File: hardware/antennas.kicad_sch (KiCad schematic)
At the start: 21 parts, among them J1001 132134

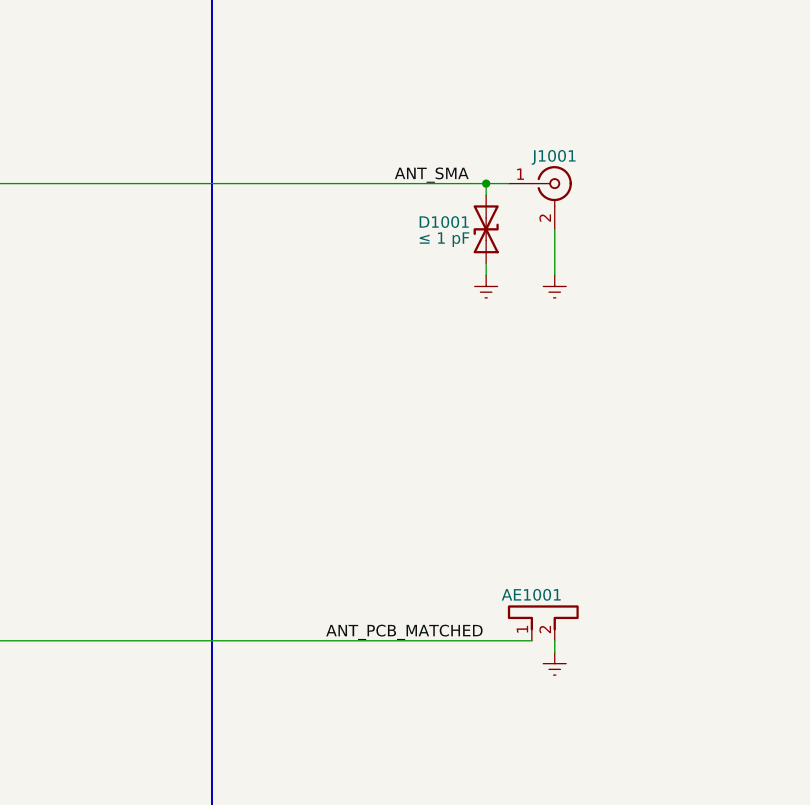
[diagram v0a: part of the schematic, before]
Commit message: HW: Update libraries, fix typos, refine schematics
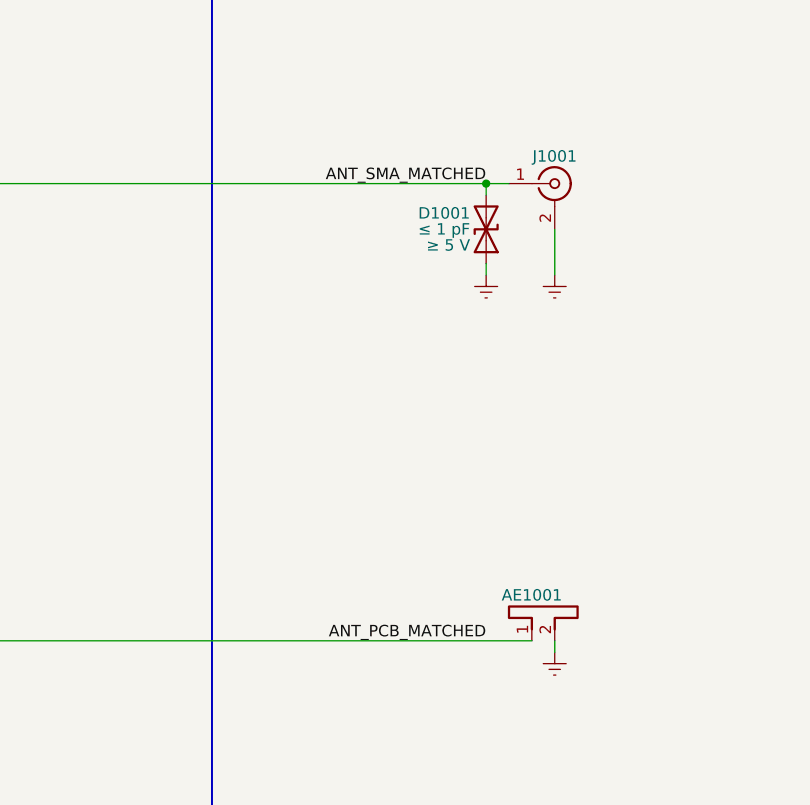
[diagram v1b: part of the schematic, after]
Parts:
- D1001: Voltage (none) -> ≥ 5 V
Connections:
- net ANT_SMA renamed ANT_SMA_MATCHED
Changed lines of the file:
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@@
 	)
 	(label "ANT_PCB_MATCHED"
-		(at 342.9 205.74 0)
+		(at 360.68 205.74 180)
 		(effects
 			(font
 				(size 1.27 1.27)
 			)
-			(justify left bottom)
+			(justify right bottom)
 		)
 	)
@@
 		)
 	)
-	(label "ANT_SMA"
-		(at 350.52 154.94 0)
+	(label "ANT_SMA_MATCHED"
+		(at 360.68 154.94 180)
 		(effects
 			(font
 				(size 1.27 1.27)
 			)
-			(justify left bottom)
+			(justify right bottom)
 		)
 	)
@@
 		(dnp no)
 		(property "Reference" "D1001"
-			(at 358.902 159.258 90)
+			(at 358.902 158.242 90)
 			(effects
 				(font
@@
 			)
 		)
-		(property "Size" ""
-			(at 358.394 162.052 90)
-			(effects
-				(font
-					(size 1.27 1.27)
-				)
-				(justify right)
-			)
-		)
-		(property "Capacitance" "≤ 1 pF"
-			(at 358.902 161.036 90)
-			(effects
-				(font
-					(size 1.27 1.27)
-				)
-				(justify right)
-			)
-		)
 		(property "Footprint review check" "+"
 			(at 360.68 160.02 90)
@@
 			)
 		)
-		(property "Power" ""
-			(at 360.68 160.02 90)
-			(effects
-				(font
-					(size 1.27 1.27)
-				)
-				(hide yes)
-			)
-		)
+		(property "Capacitance" "≤ 1 pF"
+			(at 358.902 160.02 90)
+			(effects
+				(font
+					(size 1.27 1.27)
+				)
+				(justify right)
+			)
+		)
+		(property "Voltage" "≥ 5 V"
+			(at 358.902 161.798 90)
+			(effects
+				(font
+					(size 1.27 1.27)
+				)
+				(justify right)
+			)
+		)

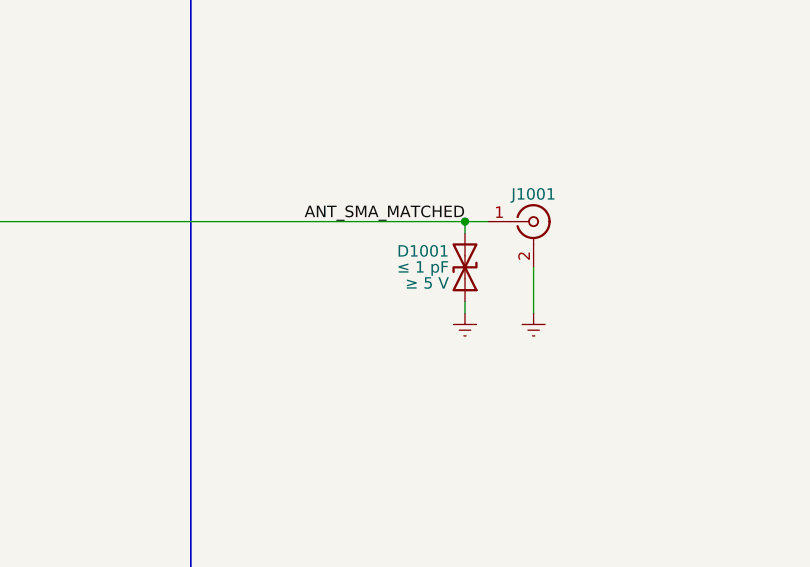
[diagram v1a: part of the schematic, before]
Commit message: HW: Update date and ANT_SMA TVS voltage rating
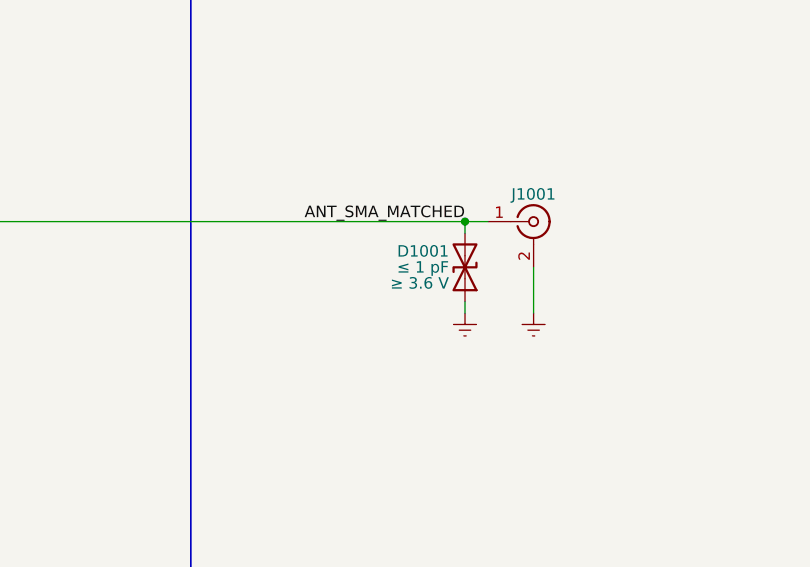
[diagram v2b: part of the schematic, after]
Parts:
- D1001: Voltage ≥ 5 V -> ≥ 3.6 V
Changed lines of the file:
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@@
 	(title_block
 		(title "Iida devkit")
-		(date "2025-05-21")
+		(date "2025-05-23")
 		(rev "v5.0.0")
 	)
@@
 			)
 		)
-		(property "Voltage" "≥ 5 V"
+		(property "Voltage" "≥ 3.6 V"
 			(at 358.902 161.798 90)
 			(effects

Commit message: HW: Refine schematics
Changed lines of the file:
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@@
 	(title_block
 		(title "Iida devkit")
-		(date "2025-05-23")
+		(date "2025-05-24")
 		(rev "v5.0.0")
 	)
@@
 	)
 	(label "ANT_SEL_PCB"
-		(at 76.2 205.74 0)
+		(at 88.9 205.74 0)
 		(effects
 			(font
@@
 	)
 	(label "ANT_SEL_SMA"
-		(at 76.2 154.94 0)
-		(effects
-			(font
+		(at 88.9 154.94 0)
+		(effects
+			(font

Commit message: HW: Fix BOM
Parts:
- C1001, C1005: DigiKey Part Number 490-11194-1-ND -> 732-13231-1-ND; MPN GJM1555C1H1R1WB01D -> 885392005006; Manufacturer Murata Electronics -> Würth Elektronik
- C1003: DigiKey Part Number 490-GJM1555C1HR33WB01DCT-ND -> 732-13226-1-ND; MPN GJM1555C1HR33WB01D -> 885392005001; Manufacturer Murata Electronics -> Würth Elektronik
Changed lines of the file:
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@@
 			)
 		)
-		(property "DigiKey Part Number" "490-11194-1-ND"
+		(property "DigiKey Part Number" "732-13231-1-ND"
 			(at 213.36 205.74 90)
 			(effects
@@
 			)
 		)
-		(property "MPN" "GJM1555C1H1R1WB01D"
+		(property "MPN" "885392005006"
 			(at 213.36 205.74 90)
 			(effects
@@
 			)
 		)
-		(property "Manufacturer" "Murata Electronics"
+		(property "Manufacturer" "Würth Elektronik"
 			(at 213.36 205.74 90)
 			(effects
@@
 			)
 		)
-		(property "DigiKey Part Number" "490-11194-1-ND"
+		(property "DigiKey Part Number" "732-13231-1-ND"
 			(at 134.62 205.74 90)
 			(effects
@@
 			)
 		)
-		(property "MPN" "GJM1555C1H1R1WB01D"
+		(property "MPN" "885392005006"
 			(at 134.62 205.74 90)
 			(effects
@@
 			)
 		)
-		(property "Manufacturer" "Murata Electronics"
+		(property "Manufacturer" "Würth Elektronik"
 			(at 134.62 205.74 90)
 			(effects
@@
 			)
 		)
-		(property "DigiKey Part Number" "490-GJM1555C1HR33WB01DCT-ND"
+		(property "DigiKey Part Number" "732-13226-1-ND"
 			(at 173.99 205.74 90)
 			(effects
@@
 			)
 		)
-		(property "MPN" "GJM1555C1HR33WB01D"
+		(property "MPN" "885392005001"
 			(at 173.99 205.74 90)
 			(effects
@@
 			)
 		)
-		(property "Manufacturer" "Murata Electronics"
+		(property "Manufacturer" "Würth Elektronik"
 			(at 173.99 205.74 90)
 			(effects

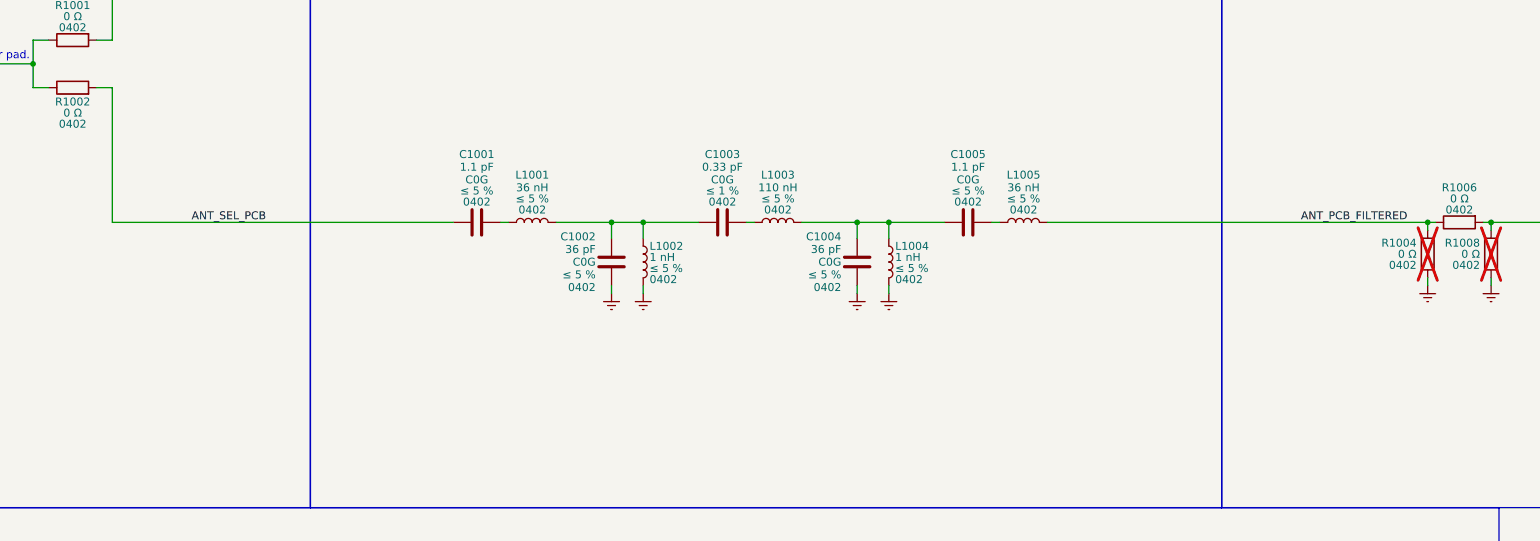
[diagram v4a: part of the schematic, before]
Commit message: HW: Fix antenna netclasses
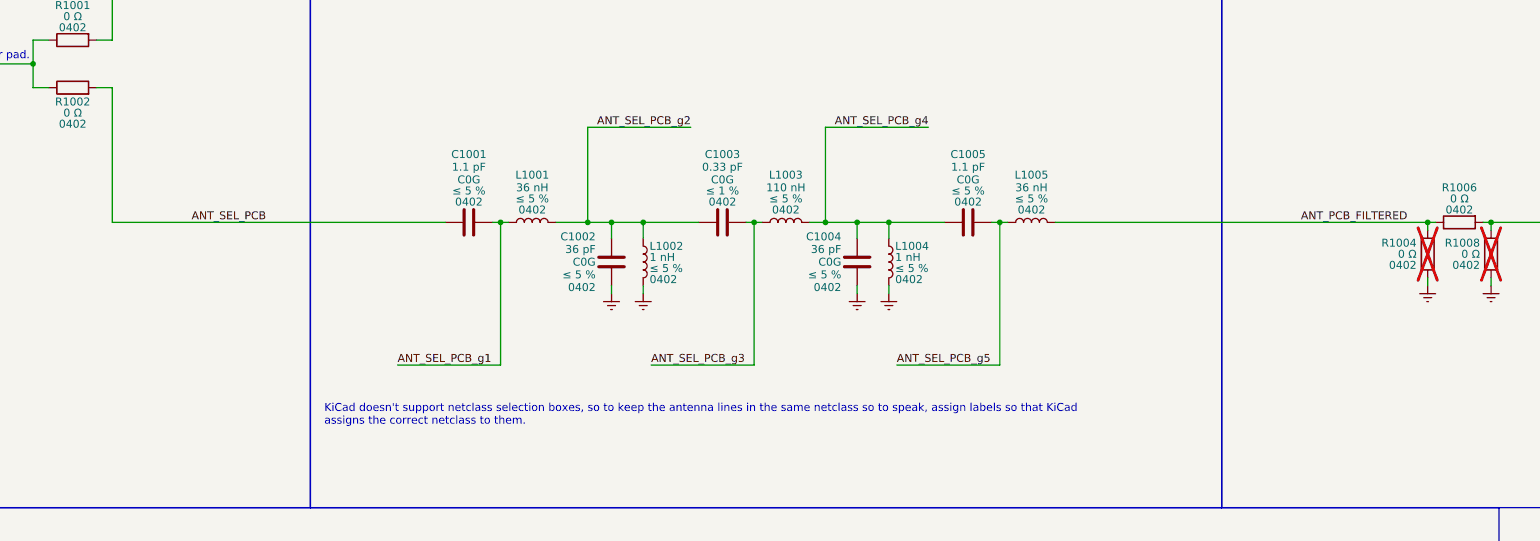
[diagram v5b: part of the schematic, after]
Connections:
- net ANT_SEL_PCB_g1: now reaches C1001.2, L1001.1
- net ANT_SEL_PCB_g2: now reaches C1002.2, C1003.1, L1001.2, L1002.2
- net ANT_SEL_PCB_g4: now reaches C1004.2, C1005.1, L1003.2, L1004.2
- net ANT_SEL_PCB_g5: now reaches C1005.2, L1005.1
- net ANT_SEL_PCB_g3: now reaches C1003.2, L1003.1
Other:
- moved on the sheet: C1001, L1003, L1005

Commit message: HW: Layout the modem section and fix footprints
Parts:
- R1003, R1004, R1007, R1008: footprint Resistor_SMD:R_0402_1005Metric -> perfect_footprints:R_0402_1005Metric
